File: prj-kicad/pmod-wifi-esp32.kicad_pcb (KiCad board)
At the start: 2 copper layers, 38.1 x 20.3 mm, 1 part, among them P1 PMOD

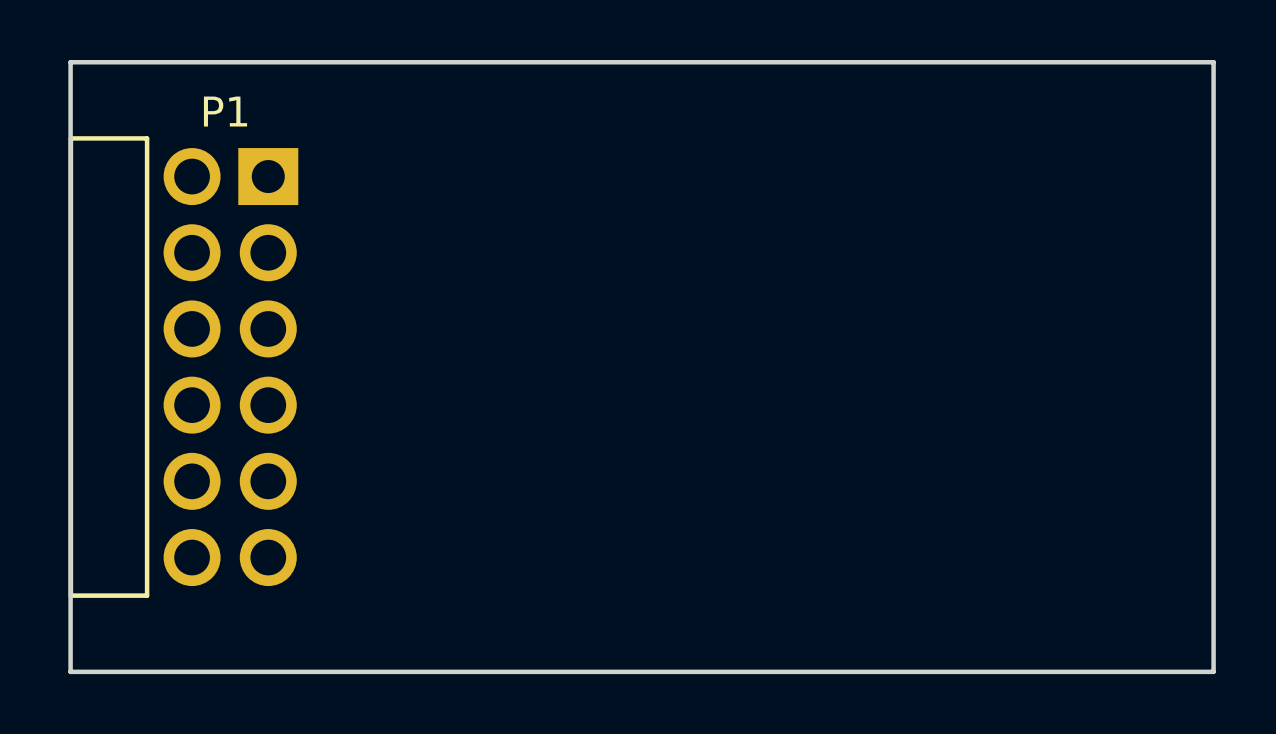
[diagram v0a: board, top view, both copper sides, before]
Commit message: = ADD: PCB routing
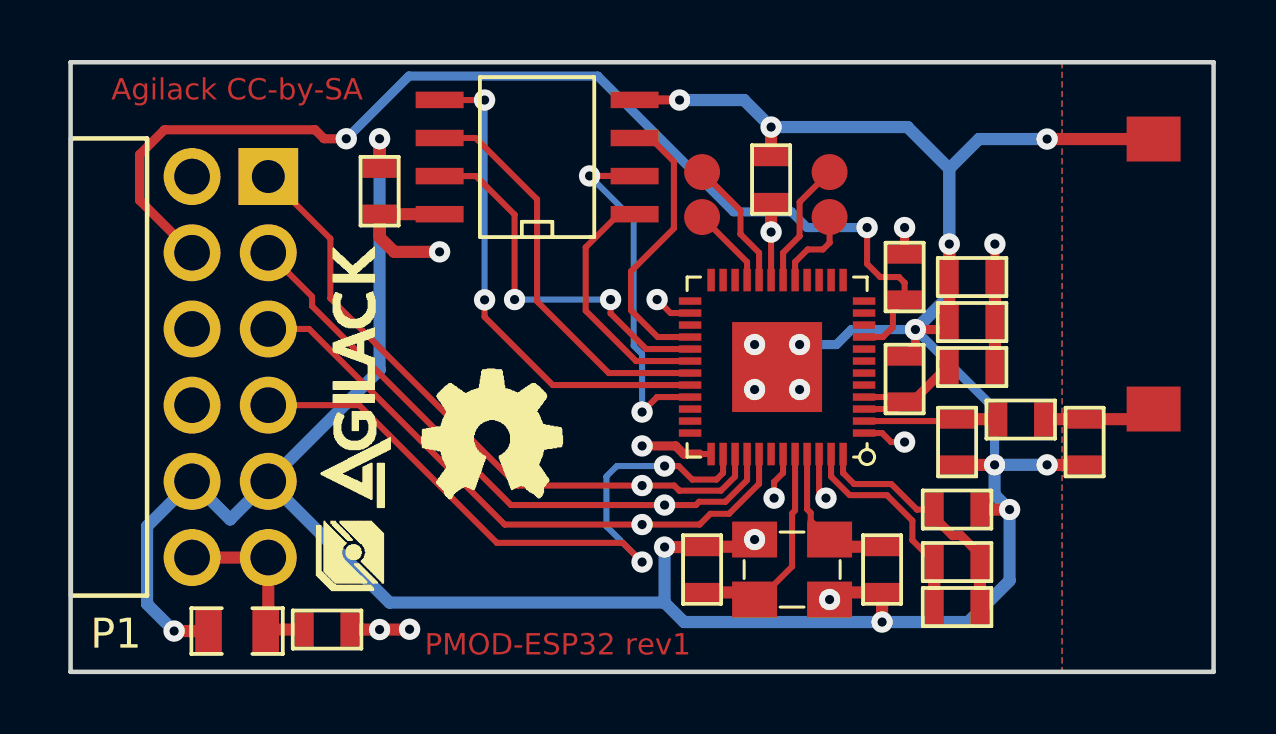
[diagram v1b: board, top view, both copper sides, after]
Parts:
- added A1: ANTENNA, pmod-wifi-esp32:ANT_7488910245, F.Cu at (165.6, 101.9)
- added C1: 10uF, pmod-wifi-esp32:SMD0805, F.Cu at (135.0, 113.8)
- added C10: 100nF, pmod-wifi-esp32:SMD0603, F.Cu at (159.5, 103.5)
- added C11: 100nF, pmod-wifi-esp32:SMD0603, F.Cu at (139.8, 99.1)
- added C12: 100nF, pmod-wifi-esp32:SMD0603, F.Cu at (152.8, 98.8)
- added C2: 10nF, pmod-wifi-esp32:SMD0603, F.Cu at (159.0, 109.8)
- added C3: 3,3nF, pmod-wifi-esp32:SMD0603, F.Cu at (159.0, 111.5)
- added C4: C, pmod-wifi-esp32:SMD0603, F.Cu at (159.0, 107.5)
- added C5: C, pmod-wifi-esp32:SMD0603, F.Cu at (163.2, 107.5)
- added C6: 10pF, pmod-wifi-esp32:SMD0603, F.Cu at (156.5, 111.8)
- added C7: 10pF, pmod-wifi-esp32:SMD0603, F.Cu at (150.5, 111.8)
- added C8: 10nF, pmod-wifi-esp32:SMD0603, F.Cu at (157.2, 105.4)
- added C9: 1uF, pmod-wifi-esp32:SMD0603, F.Cu at (159.5, 102.0)
- added FB1: FB120, pmod-wifi-esp32:SMD0603, F.Cu at (138.0, 113.8)
- added L1: INDUCTOR, pmod-wifi-esp32:SMD0603, F.Cu at (161.1, 106.8)
- added L2: INDUCTOR, pmod-wifi-esp32:SMD0603, F.Cu at (159.5, 105.0)
- added R1: 20k, pmod-wifi-esp32:SMD0603, F.Cu at (159.0, 113.0)
- added R2: 10k, pmod-wifi-esp32:SMD0603, F.Cu at (157.2, 102.0)
- added TP1: CONN_1, pmod-wifi-esp32:TP_SMD, F.Cu at (154.8, 100.0)
- added TP2: CONN_1, pmod-wifi-esp32:TP_SMD, F.Cu at (154.8, 98.5)
- added TP3: CONN_1, pmod-wifi-esp32:TP_SMD, F.Cu at (150.5, 98.5)
- added TP4: CONN_1, pmod-wifi-esp32:TP_SMD, F.Cu at (150.5, 100.0)
- added U1: ESP32, pmod-wifi-esp32:QFN48-04, F.Cu at (153.0, 105.0)
- added U2: M25P16-VME, pmod-wifi-esp32:SOIC-8, F.Cu at (145.0, 98.0)
- added X1: 40MHz, pmod-wifi-esp32:Q_3.2x2.5, F.Cu at (153.5, 111.8)
- added agilack-11.5: 450px, pmod-wifi-esp32:logo-agilack-11.5, F.Cu at (138.9, 106.3)
- added ohw_logo: VAL**, pmod-wifi-esp32:logo-ohw, F.Cu at (143.5, 107.4)
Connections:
- net Net-(P1-Pad7) renamed PMOD_IRQ
- P1 pad 1: Net-(P1-Pad1) -> PMOD_CTS
- P1 pad 11: Net-(P1-Pad11) -> GND
- P1 pad 12: Net-(P1-Pad12) -> VCC
- P1 pad 2: Net-(P1-Pad2) -> PMOD_TXD
- P1 pad 3: Net-(P1-Pad3) -> PMOD_RXD
- P1 pad 4: Net-(P1-Pad4) -> PMOD_RTS
- P1 pad 5: Net-(P1-Pad5) -> GND
- P1 pad 6: Net-(P1-Pad6) -> VCC
- P1 pad 8: Net-(P1-Pad8) -> PMOD_RST
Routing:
- net GND: track 0.00 -> 124.0 mm, vias 0 -> 18
- net +3.3V: track 0.00 -> 52.8 mm, vias 0 -> 9
- net PMOD_RST: track 0.00 -> 37.1 mm, vias 0 -> 2
- net PMOD_RTS: track 0.00 -> 22.9 mm, vias 0 -> 2
- net PMOD_CTS: track 0.00 -> 22.0 mm, vias 0 -> 1
- net PMOD_TXD: track 0.00 -> 20.8 mm, vias 0 -> 1
- net PMOD_RXD: track 0.00 -> 20.6 mm, vias 0 -> 1
- net FL_D0: track 0.00 -> 16.5 mm, vias 0 -> 2
- net +VMEM: track 0.00 -> 14.7 mm, vias 0 -> 2
- net FL_SCK: track 0.00 -> 13.6 mm
- net FL_D3: track 0.00 -> 12.7 mm, vias 0 -> 2
- net FL_D1: track 0.00 -> 11.9 mm, vias 0 -> 2
- net FL_D2: track 0.00 -> 9.53 mm
- net FL_SCS: track 0.00 -> 8.37 mm
- net Net-(C2-Pad1): track 0.00 -> 8.22 mm
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- added copper zone on In2.Cu, net +3.3V
- added copper zone on In2.Cu, net +VMEM
- added copper zone on B.Cu, net GND
- added copper zone on F.Cu, net GND
- added copper zone on In1.Cu, net GND
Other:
- copper layers 2 -> 4
- net class Default: clearance 0.2 -> 0.125
- rule trace_clearance: 0.2 -> 0.125
- board text added: "Agilack CC-by-SA"
- board text added: "JLCJLCJLCJLC"
- board text added: "PMOD-ESP32 rev1"
